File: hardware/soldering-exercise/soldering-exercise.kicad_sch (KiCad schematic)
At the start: 15 parts, among them J1 SAO v1.69bis addon, U1 NE555P

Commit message: add footprints
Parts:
- BT1: footprint (none) -> Battery:BatteryHolder_Multicomp_BC-2001_1x2032
- C11: footprint (none) -> Capacitor_SMD:C_1206_3216Metric_Pad1.33x1.80mm_HandSolder
- C12: footprint (none) -> Capacitor_THT:C_Rect_L7.0mm_W3.5mm_P2.50mm_P5.00mm
- D1, D3: footprint (none) -> LED_THT:LED_D3.0mm_Clear
- D2, D4: footprint (none) -> LED_SMD:LED_1206_3216Metric_Pad1.42x1.75mm_HandSolder
- R1, R11, R12, R3: footprint (none) -> Resistor_THT:R_Axial_DIN0309_L9.0mm_D3.2mm_P12.70mm_Horizontal
- R2, R4: footprint (none) -> Resistor_SMD:R_1206_3216Metric_Pad1.30x1.75mm_HandSolder
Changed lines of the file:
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@@
 			)
 		)
-		(property "Footprint" ""
+		(property "Footprint" "Capacitor_SMD:C_1206_3216Metric_Pad1.33x1.80mm_HandSolder"
 			(at 98.7552 99.06 0)
 			(effects
@@
 			)
 		)
-		(property "Footprint" ""
+		(property "Footprint" "Battery:BatteryHolder_Multicomp_BC-2001_1x2032"
 			(at 77.47 32.766 90)
 			(effects
@@
 			)
 		)
-		(property "Footprint" ""
+		(property "Footprint" "LED_THT:LED_D3.0mm_Clear"
 			(at 34.29 68.58 0)
 			(effects
@@
 			)
 		)
-		(property "Footprint" ""
+		(property "Footprint" "LED_SMD:LED_1206_3216Metric_Pad1.42x1.75mm_HandSolder"
 			(at 48.26 68.58 0)
 			(effects
@@
 			)
 		)
-		(property "Footprint" ""
+		(property "Footprint" "LED_THT:LED_D3.0mm_Clear"
 			(at 160.02 58.42 0)
 			(effects
@@
 			)
 		)
-		(property "Footprint" ""
+		(property "Footprint" "Resistor_THT:R_Axial_DIN0309_L9.0mm_D3.2mm_P12.70mm_Horizontal"
 			(at 140.462 68.58 90)
 			(effects
@@
 			)
 		)
-		(property "Footprint" ""
+		(property "Footprint" "Resistor_THT:R_Axial_DIN0309_L9.0mm_D3.2mm_P12.70mm_Horizontal"
 			(at 32.512 78.74 90)
 			(effects
@@
 			)
 		)
-		(property "Footprint" ""
+		(property "Footprint" "LED_SMD:LED_1206_3216Metric_Pad1.42x1.75mm_HandSolder"
 			(at 160.02 88.9 0)
 			(effects
@@
 			)
 		)
-		(property "Footprint" ""
+		(property "Footprint" "Resistor_SMD:R_1206_3216Metric_Pad1.30x1.75mm_HandSolder"
 			(at 46.482 78.74 90)
 			(effects
@@
 			)
 		)
-		(property "Footprint" ""
+		(property "Footprint" "Resistor_THT:R_Axial_DIN0309_L9.0mm_D3.2mm_P12.70mm_Horizontal"
 			(at 140.462 83.82 90)
 			(effects
@@
 			)
 		)
-		(property "Footprint" ""
+		(property "Footprint" "Resistor_SMD:R_1206_3216Metric_Pad1.30x1.75mm_HandSolder"
 			(at 158.242 78.74 90)
 			(effects
@@
 			)
 		)
-		(property "Footprint" ""
+		(property "Footprint" "Resistor_THT:R_Axial_DIN0309_L9.0mm_D3.2mm_P12.70mm_Horizontal"
 			(at 158.242 68.58 90)
 			(effects
@@
 			)
 		)
-		(property "Footprint" ""
+		(property "Footprint" "Capacitor_THT:C_Rect_L7.0mm_W3.5mm_P2.50mm_P5.00mm"
 			(at 143.2052 99.06 0)
 			(effects

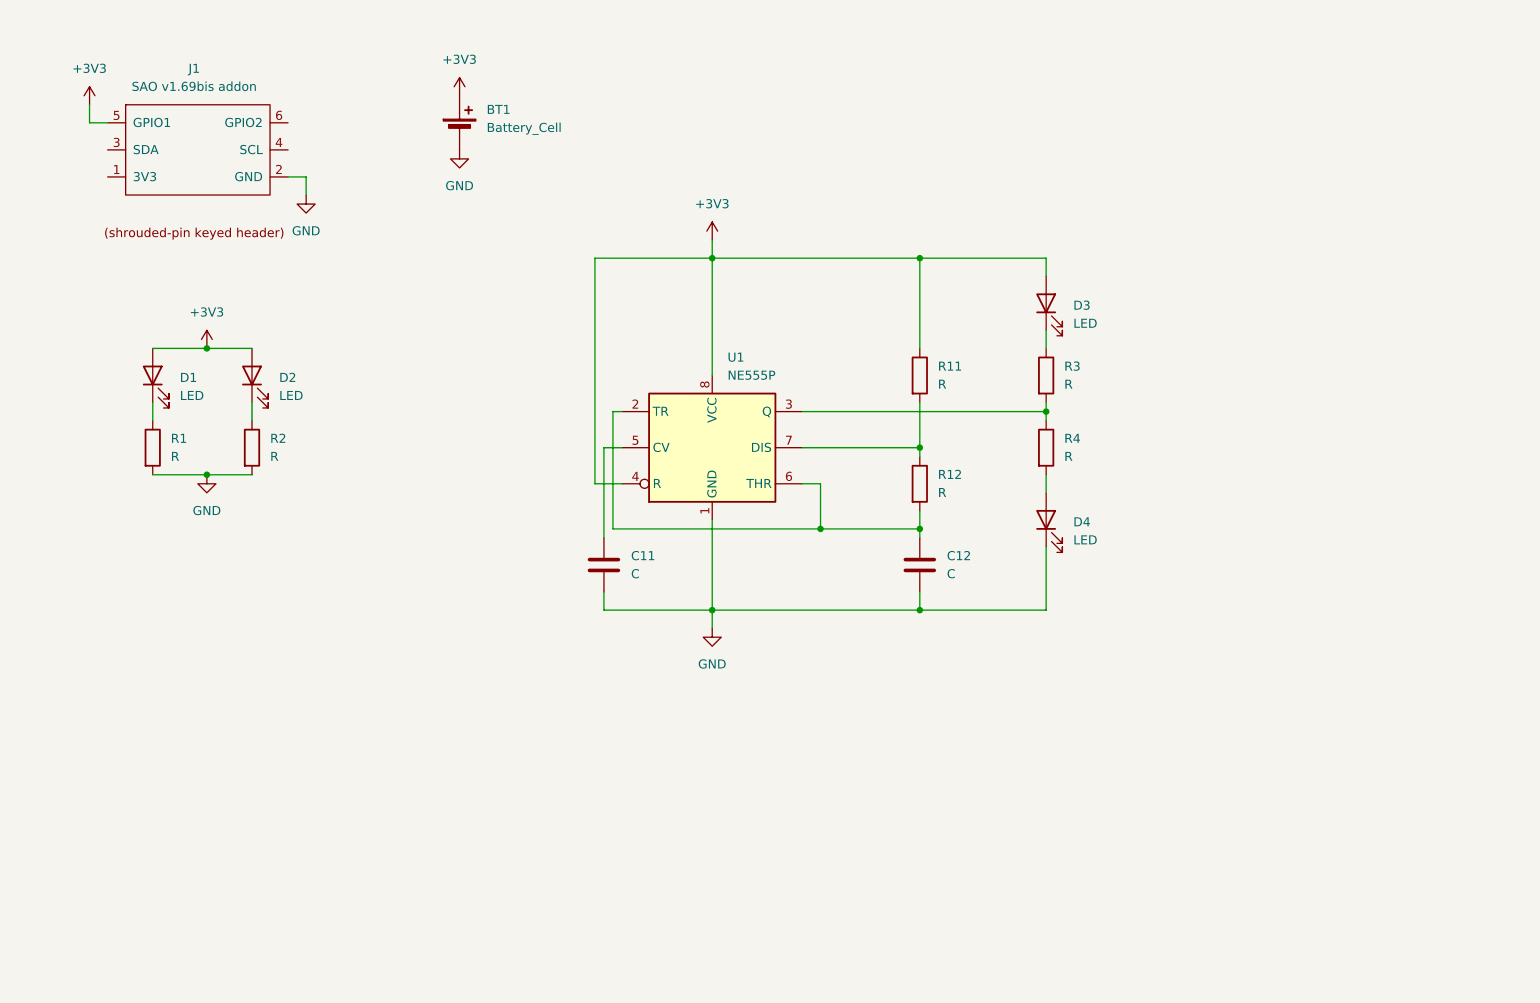
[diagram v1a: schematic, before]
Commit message: duplicate THT to SMD, layout board
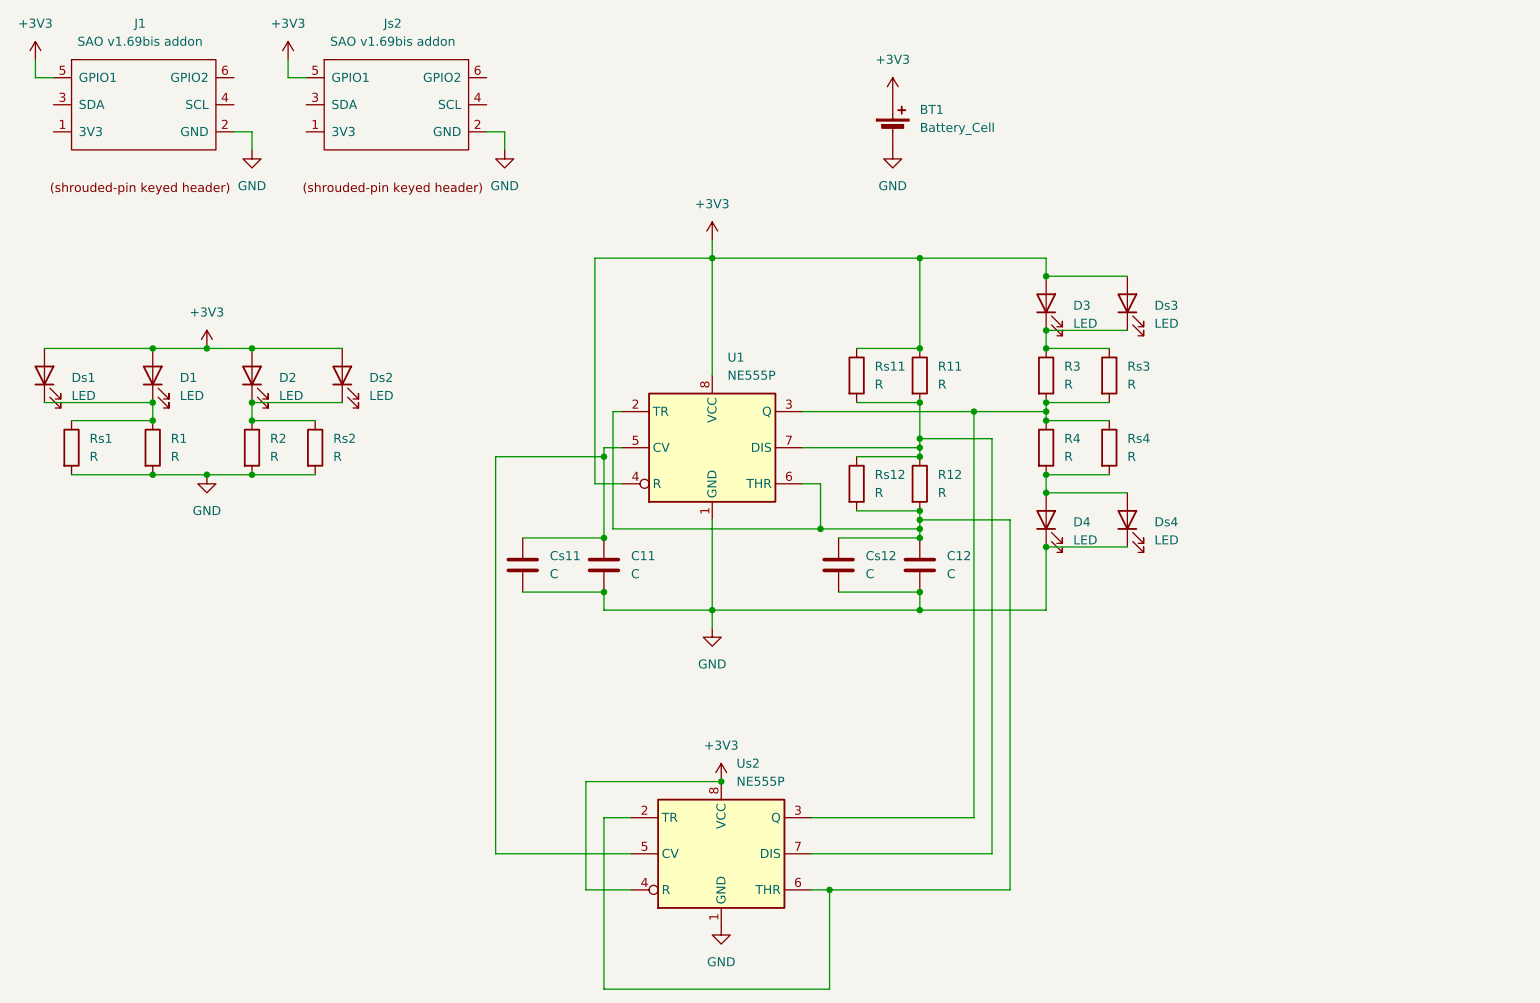
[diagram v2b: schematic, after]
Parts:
- added Cs11, Cs12: C, Capacitor_SMD:C_1206_3216Metric_Pad1.33x1.80mm_HandSolder, symbol Device:C
- added Ds1, Ds2, Ds3, Ds4: LED, LED_SMD:LED_1206_3216Metric_Pad1.42x1.75mm_HandSolder, symbol Device:LED
- added Js2: SAO v1.69bis addon, Connector_IDC:IDC-Header_2x03_P2.54mm_Vertical_SMD, symbol extra:SAO v1.69bis addon
- added Rs1, Rs11, Rs12, Rs2, Rs3, Rs4: R, Resistor_SMD:R_1206_3216Metric_Pad1.30x1.75mm_HandSolder, symbol Device:R
- added Us2: NE555P, Package_SO:SOP-8_6.605x9.655mm_P2.54mm, symbol Timer:NE555P
- C11: footprint Capacitor_SMD:C_1206_3216Metric_Pad1.33x1.80mm_HandSolder -> Capacitor_THT:C_Rect_L7.0mm_W3.5mm_P2.50mm_P5.00mm
- D2, D4: footprint LED_SMD:LED_1206_3216Metric_Pad1.42x1.75mm_HandSolder -> LED_THT:LED_D3.0mm_Clear
- R2, R4: footprint Resistor_SMD:R_1206_3216Metric_Pad1.30x1.75mm_HandSolder -> Resistor_THT:R_Axial_DIN0309_L9.0mm_D3.2mm_P12.70mm_Horizontal
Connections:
- net +3V3: now also Ds1.2 (A), Ds2.2 (A), Ds3.2 (A), Js2.5 (GPIO1), Rs11.1, Us2.4 (R), Us2.8 (VCC)
- net GND: now also Cs11.2, Cs12.2, Ds4.1 (K), Js2.2 (GND), Rs1.2, Rs2.2, Us2.1 (GND)
- net at C11.1, U1.5 (CV): now also Cs11.1, Us2.5 (CV)
- net at D1.1 (K), R1.1: now also Ds1.1 (K), Rs1.1
- net at D2.1 (K), R2.1: now also Ds2.1 (K), Rs2.1
- net at C12.1, R12.2, U1.2 (TR)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: now also Cs12.1, Rs12.2, Us2.2 (TR), Us2.6 (THR)
- net at R3.2, R4.1, U1.3 (Q): now also Rs3.2, Rs4.1, Us2.3 (Q)
- net at R11.2, R12.1, U1.7 (DIS): now also Rs11.2, Rs12.1, Us2.7 (DIS)
- net at D3.1 (K), R3.1: now also Ds3.1 (K), Rs3.1
- net at D4.2 (A), R4.2: now also Ds4.2 (A), Rs4.2
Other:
- moved on the sheet: BT1, J1

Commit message: document values
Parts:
- C11, C12, Cs11, Cs12: value C -> 10n
- R1, R2, R3, R4, Rs1, Rs2, Rs3, Rs4: value R -> 22
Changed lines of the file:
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@@
 	(generator_version "9.0")
 	(paper "A4")
+	(text_box "allaboutcircuits.com/tools/555-timer-astable-circuit\n\nC12: 10n, 56n, 270n\nR11, R12: 560k, 910k, 4M7"
+		(exclude_from_sim no)
+		(at 161.29 106.68 0)
+		(size 64.77 10.16)
+		(margins 0.9525 0.9525 0.9525 0.9525)
+		(stroke
+			(width 0)
+			(type solid)
+		)
+		(fill
+			(type none)
+		)
+		(effects
+			(font
+				(size 1.27 1.27)
+			)
+			(justify left top)
+		)
+	)
 	(junction
 		(at 48.26 64.77)
@@
 			)
 		)
-		(property "Value" "C"
+		(property "Value" "10n"
 			(at 101.6 96.5199 0)
 			(effects
@@
 			)
 		)
-		(property "Value" "C"
+		(property "Value" "10n"
 			(at 90.17 96.5199 0)
 			(effects
@@
 			)
 		)
-		(property "Value" "R"
+		(property "Value" "22"
 			(at 171.45 69.8499 0)
 			(effects
@@
 			)
 		)
-		(property "Value" "C"
+		(property "Value" "10n"
 			(at 134.62 96.5199 0)
 			(effects
@@
 			)
 		)
-		(property "Value" "R"
+		(property "Value" "22"
 			(at 36.83 80.0099 0)
 			(effects
@@
 			)
 		)
-		(property "Value" "R"
+		(property "Value" "22"
 			(at 171.45 80.0099 0)
 			(effects
@@
 			)
 		)
-		(property "Value" "R"
+		(property "Value" "22"
 			(at 50.8 80.0099 0)
 			(effects
@@
 			)
 		)
-		(property "Value" "R"
+		(property "Value" "22"
 			(at 162.56 80.0099 0)
 			(effects
@@
 			)
 		)
-		(property "Value" "R"
+		(property "Value" "22"
 			(at 59.69 80.0099 0)
 			(effects
@@
 			)
 		)
-		(property "Value" "R"
+		(property "Value" "22"
 			(at 25.4 80.0099 0)
 			(effects
@@
 			)
 		)
-		(property "Value" "R"
+		(property "Value" "22"
 			(at 162.56 69.8499 0)
 			(effects
@@
 			)
 		)
-		(property "Value" "C"
+		(property "Value" "10n"
 			(at 146.05 96.5199 0)
 			(effects

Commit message: added PhreakNIC logo
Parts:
- Cs12: value 10n -> C
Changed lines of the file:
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@@
 			)
 		)
-		(property "Value" "10n"
+		(property "Value" "C"
 			(at 134.62 96.5199 0)
 			(effects
